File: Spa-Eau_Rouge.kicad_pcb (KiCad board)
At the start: 4 copper layers, 50 x 50 mm, 51 parts, among them J1 XT30PW-M, J2 PH1RA-03-UA, J3 SM02B-GHS-TB, J4 1985807, Q1 DMN3731U-7, U1 113991054, U2 SN74LVC1G17DBVR, U3 LMR51420YDDCR, U4 LM317MDCYR

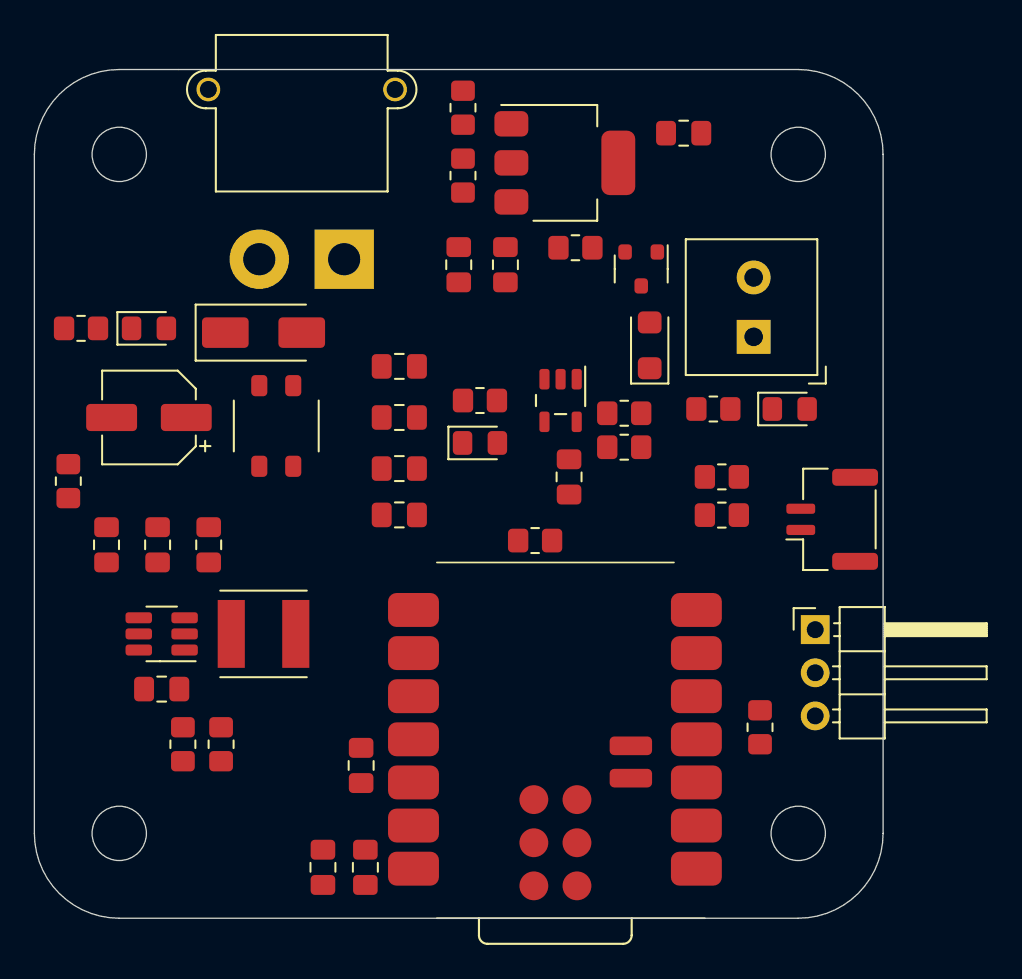
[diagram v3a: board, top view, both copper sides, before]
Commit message: pcb routing completed
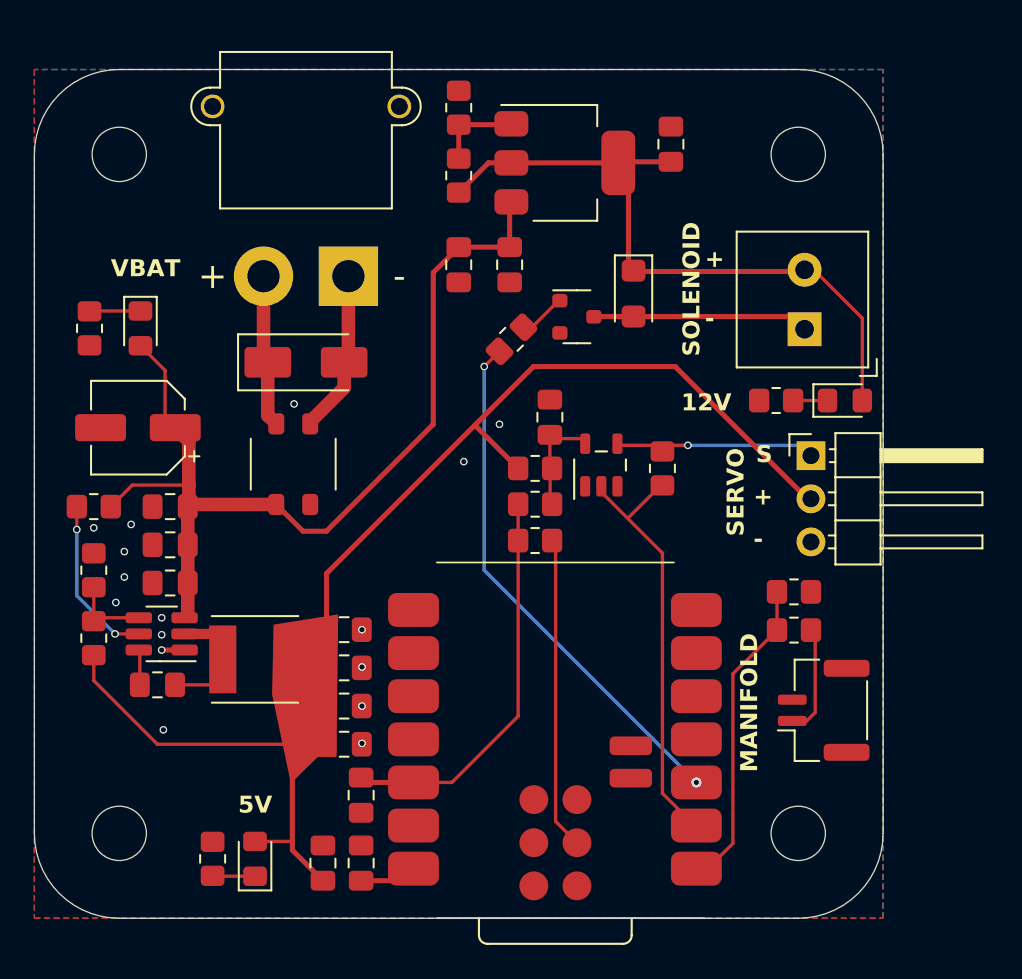
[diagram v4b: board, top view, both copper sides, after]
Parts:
- moved R10 31.3 mm to (110.5, 146.5), turned to 90 degrees
- moved D3 27.9 mm to (113.0, 146.5), turned to 90 degrees
- moved C10 20.3 mm to (118.2, 137.5)
- moved R6 16.3 mm to (137.0, 123.5)
- moved C13 13.9 mm to (118.2, 139.8)
- moved C11 12.9 mm to (118.2, 133.0)
- moved R11 12.7 mm to (103.5, 129.5), turned to 90 degrees
- moved C12 12.2 mm to (118.2, 135.2)
- moved J3 11.3 mm to (146.5, 137.8)
- moved J2 10.3 mm to (145.8, 122.8)
- moved R9 8.16 mm to (103.5, 133.5)
- moved R1 8.00 mm to (144.8, 133.0), turned to 180 degrees
- moved R2 8.00 mm to (144.8, 130.8)
- moved R4 7.50 mm to (129.5, 125.6), turned to 0 degrees
- moved R15 6.58 mm to (128.1, 115.9), turned to 45 degrees
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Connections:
- FL1 pad 1: +BATT -> VBAT_FILTERED
- FL1 pad 2: -BATT -> GND
- FL1 pad 3: GND -> -BATT
- FL1 pad 4: VBAT_FILTERED -> +BATT
- J4 pad 1: +12V -> SOLENOID-
- J4 pad 2: SOLENOID- -> +12V
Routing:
- net +5V: track 0.00 -> 75.8 mm
- net VBAT_FILTERED: track 0.00 -> 57.0 mm
- net +12V: track 0.00 -> 39.3 mm
- net /SOLENOID_DRIVE: track 0.00 -> 31.0 mm, vias 0 -> 2
- net /MCU/RAW_SERVO_PWM: track 0.00 -> 25.5 mm
- net +3.3V: track 0.00 -> 23.5 mm
- net /MCU/RELEASE_TRIGGER_3.3V: track 0.00 -> 18.7 mm
- net /MCU/CHIP_EN: track 0.00 -> 18.4 mm
- net /BUFF_SERVO_PWM: track 0.00 -> 12.5 mm, vias 0 -> 1
- net SOLENOID-: track 0.00 -> 12.5 mm
- net /Power/EN: track 0.00 -> 9.83 mm, vias 0 -> 2
- net -BATT: track 0.00 -> 9.63 mm
- net +BATT: track 0.00 -> 9.01 mm
- net /Power/SW: track 0.00 -> 8.06 mm
- net /RELEASE_TRIGGER: track 0.00 -> 6.51 mm
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- added copper zone on B.Cu, net GND
- added copper zone on F.Cu, net GND
- added copper zone on In1.Cu, net GND
- added copper zone on In2.Cu, net GND
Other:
- board text added: "+"
- board text added: "-"
- board text added: "12V"
- board text added: "5V"
- board text added: "MANIFOLD"
- board text added: "S"
- board text added: "SERVO"
- board text added: "SOLENOID"
- board text added: "VBAT"

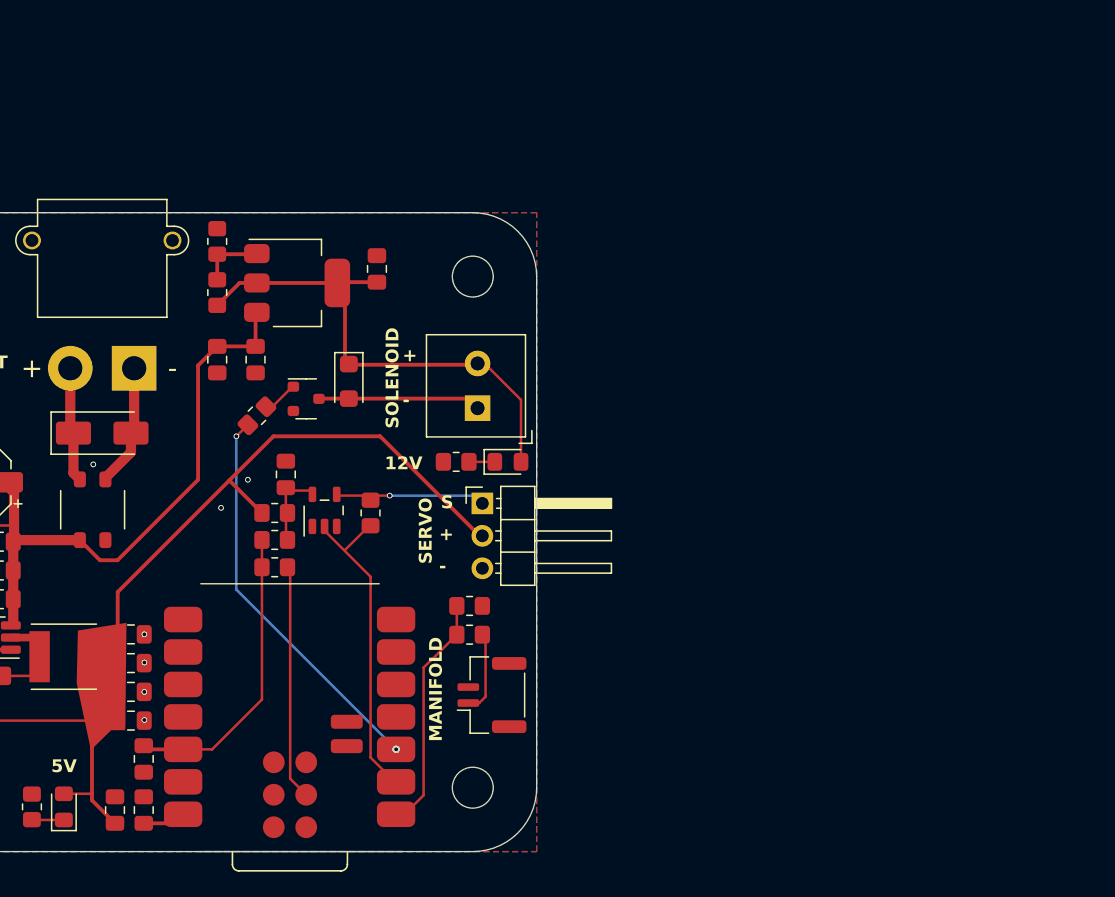
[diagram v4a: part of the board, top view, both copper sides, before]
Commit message: added i2c + another servo rail
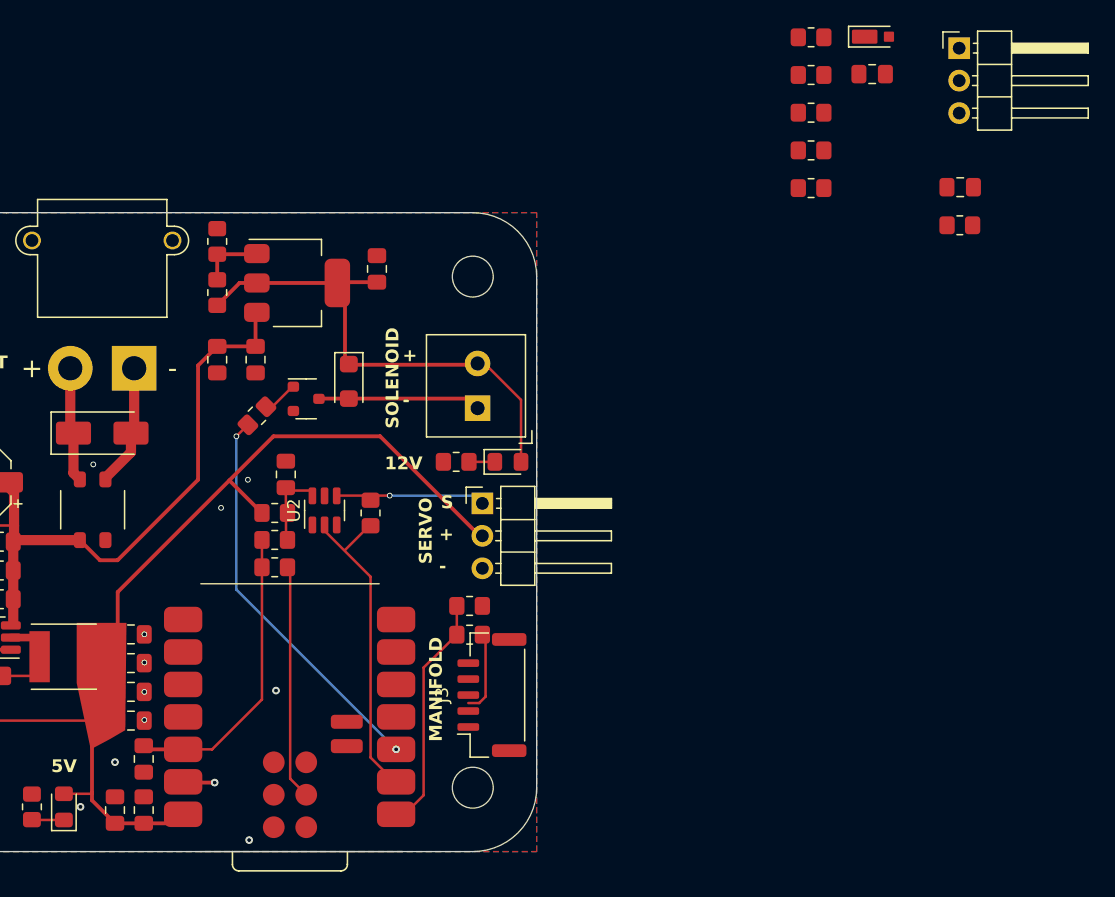
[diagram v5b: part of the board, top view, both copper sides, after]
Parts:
- added C17: DNP, Capacitor_SMD:C_0805_2012Metric_Pad1.18x1.45mm_HandSolder, F.Cu at (183.1, 98.0)
- added C18: CL21B105KAFNNNE, Capacitor_SMD:C_0805_2012Metric_Pad1.18x1.45mm_HandSolder, F.Cu at (176.3, 89.2)
- added D6: MSS1P3L-M3/89A, Diode_SMD:D_MicroSMP_AK_MSS1P3L-M3_89A, F.Cu at (176.6, 86.2)
- added J5: PH1RA-03-UA, Connector_PinHeader_2.54mm:PinHeader_1x03_P2.54mm_Horizontal, F.Cu at (183.1, 87.1)
- added R16: DNP 0805, Resistor_SMD:R_0805_2012Metric_Pad1.20x1.40mm_HandSolder, F.Cu at (183.1, 101.0)
- added R17: DNP 0805, Resistor_SMD:R_0805_2012Metric_Pad1.20x1.40mm_HandSolder, F.Cu at (171.5, 86.3)
- added R18: DNP 0805, Resistor_SMD:R_0805_2012Metric_Pad1.20x1.40mm_HandSolder, F.Cu at (171.5, 89.2)
- added R19: DNP 0805, Resistor_SMD:R_0805_2012Metric_Pad1.20x1.40mm_HandSolder, F.Cu at (171.5, 92.2)
- added R22: RMCF0805JT4K70, Resistor_SMD:R_0805_2012Metric_Pad1.20x1.40mm_HandSolder, F.Cu at (171.5, 95.1)
- added R23: RMCF0805JT4K70, Resistor_SMD:R_0805_2012Metric_Pad1.20x1.40mm_HandSolder, F.Cu at (171.5, 98.1)
- J3: value SM02B-GHS-TB -> SM05B-GHS-TB; footprint Connector_JST:JST_GH_SM02B-GHS-TB_1x02-1MP_P1.25mm_Horizontal -> Connector_JST:JST_GH_SM05B-GHS-TB_1x05-1MP_P1.25mm_Horizontal
- R2: value DNP 0805 -> RC0805JR-070RL
- U2: value SN74LVC1G17DBVR -> SN74LVC2G17DBVR; footprint Package_TO_SOT_SMD:SOT-23-5_SN74LVC1G17DBVR -> Package_TO_SOT_SMD:SOT-23-6
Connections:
- C1 pad 1: +5V -> MCU_5V
- C2 pad 1: +5V -> MCU_5V
- J2 pad 1: /BUFF_SERVO_PWM -> /BUFF_SERVO_PWM2
- J3 pad 1: /RELEASE_TRIGGER -> /DJI_PWM1
- J3 pad 2: GND -> /DJI_PWM2
- R1 pad 1: /RELEASE_TRIGGER -> /DJI_PWM1
- R1 pad 2: /MCU/RELEASE_TRIGGER_3.3V -> /MCU/RAW_SERVO_PWM1
- R2 pad 1: /MCU/RELEASE_TRIGGER_3.3V -> /DJI_PWM2
- R2 pad 2: GND -> /MCU/RAW_SERVO_PWM2
- R6 pad 1: /MCU/RAW_SERVO_PWM -> /DJI_PWM1
- R6 pad 2: /BUFF_SERVO_PWM -> /BUFF_SERVO_PWM1
- U1 pad 1: /MCU/RELEASE_TRIGGER_3.3V -> unconnected-(U1-GPIO2_A0_D0-Pad1)
- U1 pad 14: +5V -> MCU_5V
- U1 pad 2: /MCU/RAW_SERVO_PWM -> /MCU/ESP32_PWM1
- U1 pad 3: /SOLENOID_DRIVE -> /MCU/ESP32_PWM2
- U1 pad 4: unconnected-(U1-GPIO5_A3_D3-Pad4) -> /SOLENOID_DRIVE
- U1 pad 5: unconnected-(U1-GPIO6_D4_SDA-Pad5) -> /SDA
- U1 pad 6: unconnected-(U1-GPIO7_D5_SCL-Pad6) -> /SCL
- U2 pad 1: GND -> /MCU/RAW_SERVO_PWM1
- U2 pad 2: /MCU/RAW_SERVO_PWM -> GND
- U2 pad 3: GND -> /MCU/RAW_SERVO_PWM2
- U2 pad 4: /BUFF_SERVO_PWM -> /BUFF_SERVO_PWM2
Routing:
- net /MCU/RELEASE_TRIGGER_3.3V: track 18.7 -> 0.00 mm
- net (no net): track 0.00 -> 18.7 mm
- net /RELEASE_TRIGGER: track 6.51 -> 0.00 mm
- net /DJI_PWM1: track 0.00 -> 6.51 mm
- net GND: track 1.35 -> 3.84 mm, vias 16 -> 21
- net +5V: track 75.8 -> 78.1 mm
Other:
- board text removed: "${REFERENCE}"

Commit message: 2nd rev is done
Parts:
- removed R22, R23: RMCF0805JT4K70, Resistor_SMD:R_0805_2012Metric_Pad1.20x1.40mm_HandSolder
- added G***: LOGO, LOGO, B.Cu at (126.2, 130.4)
- added G***: LOGO, LOGO, B.Cu at (123.1, 130.4)
- added Q2: DMN3731U-7, Package_TO_SOT_SMD:SOT-23-3_DMN3731U-7, F.Cu at (141.2, 140.2)
- added R20: ERJ-P06J112V, Resistor_SMD:R_0805_2012Metric_Pad1.20x1.40mm_HandSolder, F.Cu at (140.9, 143.9)
- added R21: RC0805JR-070RL, Resistor_SMD:R_0805_2012Metric_Pad1.20x1.40mm_HandSolder, F.Cu at (145.1, 141.1)
- C10: value GRM21BR61C106KE15K -> CL21B104KBCNNNC
- C14: value GRM21BR61H475KE51L -> GRM21BR61C106KE15K
- C15: value CL21B104KBCNNNC -> DNP
- C17: value DNP -> CL21B104KBCNNNC
- C18: value CL21B105KAFNNNE -> GRM21BR61H475KE51L
- C4: value CL21B104KBCNNNC -> CL21B105KAFNNNE
- C5: value 865080642006 -> CL21B104KBCNNNC; footprint Capacitor_SMD:865080642006 -> Capacitor_SMD:C_0805_2012Metric_Pad1.18x1.45mm_HandSolder
- C6: value CL21B104KBCNNNC -> 865080642006; footprint Capacitor_SMD:C_0805_2012Metric_Pad1.18x1.45mm_HandSolder -> Capacitor_SMD:865080642006
- C7: value GRM21BR61H475KE51L -> CL21B104KBCNNNC
- C9: value CL21B104KBCNNNC -> GRM21BR61H475KE51L
- D1: value 150080GS75000 -> MSS1P3L-M3/89A; footprint LED_SMD:LED_0805_2012Metric_Pad1.15x1.40mm_HandSolder -> Diode_SMD:D_MicroSMP_AK_MSS1P3L-M3_89A
- D5: value STPS2H100ZF -> 150080GS75000; footprint Diode_SMD:D_SOD-123F_STPS2H100ZF -> LED_SMD:LED_0805_2012Metric_Pad1.15x1.40mm_HandSolder
- D6: value MSS1P3L-M3/89A -> STPS2H100ZF; footprint Diode_SMD:D_MicroSMP_AK_MSS1P3L-M3_89A -> Diode_SMD:D_SOD-123F_STPS2H100ZF
- J2: value PH1RA-03-UA -> SM05B-GHS-TB; footprint Connector_PinHeader_2.54mm:PinHeader_1x03_P2.54mm_Horizontal -> Connector_JST:JST_GH_SM05B-GHS-TB_1x05-1MP_P1.25mm_Horizontal
- J3: value SM05B-GHS-TB -> 1985807; footprint Connector_JST:JST_GH_SM05B-GHS-TB_1x05-1MP_P1.25mm_Horizontal -> TerminalBlock_Phoenix:TerminalBlock_Phoenix_MKDS-1,5-2_1x02_P3.50mm_Horizontal_1985807
- J4: value 1985807 -> PH1RA-03-UA; footprint TerminalBlock_Phoenix:TerminalBlock_Phoenix_MKDS-1,5-2_1x02_P3.50mm_Horizontal_1985807 -> Connector_PinHeader_2.54mm:PinHeader_1x03_P2.54mm_Horizontal
- R1, R2: value RC0805JR-070RL -> RMCF0805JT4K70
- R10: value RC0805FR-0790R9L -> RC0805JR-070RL
- R11: value RT0805BRD0715KL -> DNP 0805
- R12: value RT0805BRD071K3L -> ERJ-P06J112V
- R13, R7: value ERJ-P06J112V -> RC0805JR-070RL
- R14: value RT0805BRD0710K7L -> ERA-6AEB114V
- R15: value RC0805JR-070RL -> RT0805BRD0715KL
- R16: value DNP 0805 -> RC0805FR-0790R9L
- R18: value DNP 0805 -> RT0805BRD071K3L
- R19: value DNP 0805 -> RT0805BRD0710K7L
- R8: value RC0805JR-070RL -> DNP 0805
- R9: value ERA-6AEB114V -> DNP 0805
- moved C17 75.0 mm to (120.2, 138.7), turned to 180 degrees
- moved R18 67.6 mm to (125.2, 138.5)
- moved C18 66.9 mm to (132.8, 140.0)
- moved D6 66.5 mm to (137.2, 139.8)
- moved R19 62.9 mm to (129.0, 138.5)
- moved R17 61.5 mm to (135.2, 135.9), turned to -90 degrees
- moved J5 58.5 mm to (145.8, 132.2)
- moved H3 58.0 mm to (146.0, 104.0)
- moved C1 48.8 mm to (138.0, 102.8)
- moved C2 48.7 mm to (140.1, 102.8)
- moved R1 43.8 mm to (112.2, 103.7), turned to -90 degrees
- moved J2 43.5 mm to (103.3, 113.5), turned to -90 degrees
- moved R16 42.2 mm to (145.0, 119.1), turned to -90 degrees
- moved H1 41.0 mm to (104.0, 146.0)
- moved H2 41.0 mm to (104.0, 104.0)
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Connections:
- C10 pad 1: +5V -> VBAT_FILTERED
- C14 pad 1: VBAT_FILTERED -> +5V
- C15 pad 1: VBAT_FILTERED -> /Power/SW_SNUBBER
- C16 pad 1: +12V -> VBAT_FILTERED
- C17 pad 1: /Power/SW_SNUBBER -> VBAT_FILTERED
- C18 pad 1: +3.3V -> +12V
- C4 pad 1: /MCU/VCC_BUFFER -> +3.3V
- C5 pad 1: VBAT_FILTERED -> /MCU/VCC_BUFFER
- C6 pad 1: /Power/BOOT -> VBAT_FILTERED
- C6 pad 2: /Power/SW -> GND
- C7 pad 1: VBAT_FILTERED -> /Power/BOOT
- C7 pad 2: GND -> /Power/SW
- D1 pad 1: /Power/VIN_LED_K -> MCU_5V
- D1 pad 2: VBAT_FILTERED -> +5V
- D3 pad 1: /Power/5V_LED_K -> /Power/VIN_LED_K
- D3 pad 2: +5V -> +BATT
- D4 pad 1: /Power/12V_LED_K -> /Power/5V_LED_K
- D4 pad 2: +12V -> +5V
- D5 pad 1: +12V -> /Power/12V_LED_K
- D5 pad 2: SOLENOID- -> +12V
- D6 pad 1: MCU_5V -> +12V
- D6 pad 2: +5V -> SOLENOID-
- J2 pad 1: /BUFF_SERVO_PWM2 -> /DJI_PWM1
- J2 pad 2: +5V -> /DJI_PWM2
- J2 pad 3: GND -> /SDA
- J3 pad 1: /DJI_PWM1 -> +12V
- J3 pad 2: /DJI_PWM2 -> SOLENOID-
- J4 pad 1: SOLENOID- -> /BUFF_SERVO_PWM1
- J4 pad 2: +12V -> +5V
- J5 pad 1: /BUFF_SERVO_PWM1 -> /BUFF_SERVO_PWM2
- Q1 pad 1: /Solenoid Driver/SOLENOID_FET_G -> /MCU/VIN_LED_CONTROL
- Q1 pad 3: SOLENOID- -> /Power/VIN_LED_FET_D
- R1 pad 1: /DJI_PWM1 -> +3.3V
- R1 pad 2: /MCU/RAW_SERVO_PWM1 -> /SDA
- R10 pad 1: /Power/5V_LED_K -> /DJI_PWM2
- R10 pad 2: GND -> /MCU/RAW_SERVO_PWM2
- R11 pad 1: /Power/FB -> /MCU/ESP32_PWM2
- R11 pad 2: GND -> /MCU/RAW_SERVO_PWM2
- R12 pad 1: +12V -> /Power/VIN_LED_K
- R12 pad 2: /Power/ADJ -> /Power/VIN_LED_FET_D
- R13 pad 1: /Power/12V_LED_K -> VBAT_FILTERED
- R13 pad 2: GND -> /Power/EN
- R14 pad 1: /Power/ADJ -> +5V
- R14 pad 2: GND -> /Power/FB
- R15 pad 1: /SOLENOID_DRIVE -> /Power/FB
- R15 pad 2: /Solenoid Driver/SOLENOID_FET_G -> GND
- R16 pad 1: /Power/SW -> /Power/5V_LED_K
- R16 pad 2: /Power/SW_SNUBBER -> GND
- R17 pad 1: /MCU/ESP32_PWM1 -> /Power/SW
- R17 pad 2: /MCU/RAW_SERVO_PWM1 -> /Power/SW_SNUBBER
- R18 pad 1: /DJI_PWM2 -> +12V
- R18 pad 2: /BUFF_SERVO_PWM2 -> /Power/ADJ
- R19 pad 1: /MCU/ESP32_PWM2 -> /Power/ADJ
- R19 pad 2: /MCU/RAW_SERVO_PWM2 -> GND
- R2 pad 1: /DJI_PWM2 -> +3.3V
- R2 pad 2: /MCU/RAW_SERVO_PWM2 -> /SCL
- R7 pad 1: /Power/VIN_LED_K -> /DJI_PWM1
- R7 pad 2: GND -> /MCU/RAW_SERVO_PWM1
- R8 pad 1: VBAT_FILTERED -> /MCU/ESP32_PWM1
- R8 pad 2: /Power/EN -> /MCU/RAW_SERVO_PWM1
- R9 pad 1: +5V -> /DJI_PWM2
- R9 pad 2: /Power/FB -> /BUFF_SERVO_PWM2
- U1 pad 7: unconnected-(U1-GPIO21_D6_TX-Pad7) -> /MCU/VIN_LED_CONTROL
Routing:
- net /BUFF_SERVO_PWM1: track 0.00 -> 48.9 mm, vias 0 -> 2
- net /BUFF_SERVO_PWM2: track 0.00 -> 47.0 mm, vias 0 -> 2
- net /SCL: track 0.00 -> 41.3 mm, vias 0 -> 3
- net +3.3V: track 23.5 -> 54.3 mm
- net /SDA: track 0.00 -> 29.6 mm, vias 0 -> 2
- net VBAT_FILTERED: track 57.0 -> 27.6 mm
- net /MCU/RAW_SERVO_PWM: track 25.5 -> 0.00 mm
- net /MCU/VIN_LED_CONTROL: track 0.00 -> 24.1 mm, vias 0 -> 2
- net /SOLENOID_DRIVE: track 31.0 -> 54.2 mm
- net /MCU/RAW_SERVO_PWM1: track 0.00 -> 19.2 mm
- net (no net): track 18.7 -> 0.00 mm
- net /MCU/RAW_SERVO_PWM2: track 0.00 -> 17.5 mm
- net +BATT: track 9.01 -> 26.0 mm
- net /BUFF_SERVO_PWM: track 12.5 -> 0.00 mm, vias 1 -> 0
- net /Power/FB: track 4.73 -> 13.2 mm
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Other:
- outline, holes or cut-outs redrawn
- board text added: "DJI"
- board text added: "Jan 2025"
- board text added: "Jerry Tian"
- board text added: "SERVO1"
- board text added: "SERVO2"
- board text added: "SYDE 2025"
- board text added: "if this PCB was an F1 car it'd need a safety car every time it tries to power up"
- board text removed: "MANIFOLD"
- board text removed: "SERVO"

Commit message: added new memes
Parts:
- added G***: LOGO, LOGO, B.Cu at (106.2, 124.9)
- added G***: LOGO, LOGO, B.Cu at (106.0, 114.2)
- moved G*** 11.4 mm to (132.2, 123.6), turned to 90 degrees
- moved G*** 10.4 mm to (131.8, 121.6), turned to 90 degrees
